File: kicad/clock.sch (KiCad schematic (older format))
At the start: 42 parts, among them Q1 PN2222A, Q2 PN2222A, Q3 PN2222A, Q4 PN2222A, Q5 PN2222A, Q6 PN2222A, U1 74HC04, U10 7SEGMENT_CC, U11 4543, U12 7SEGMENT_CC, U13 4543, U14 7SEGMENT_CC, U2 74LS390, U3 CD4060, U4 4543, U5 7SEGMENT_CC, U6 4027, U7 74LS390, U8 74LS390, U9 4543, Y1 32768

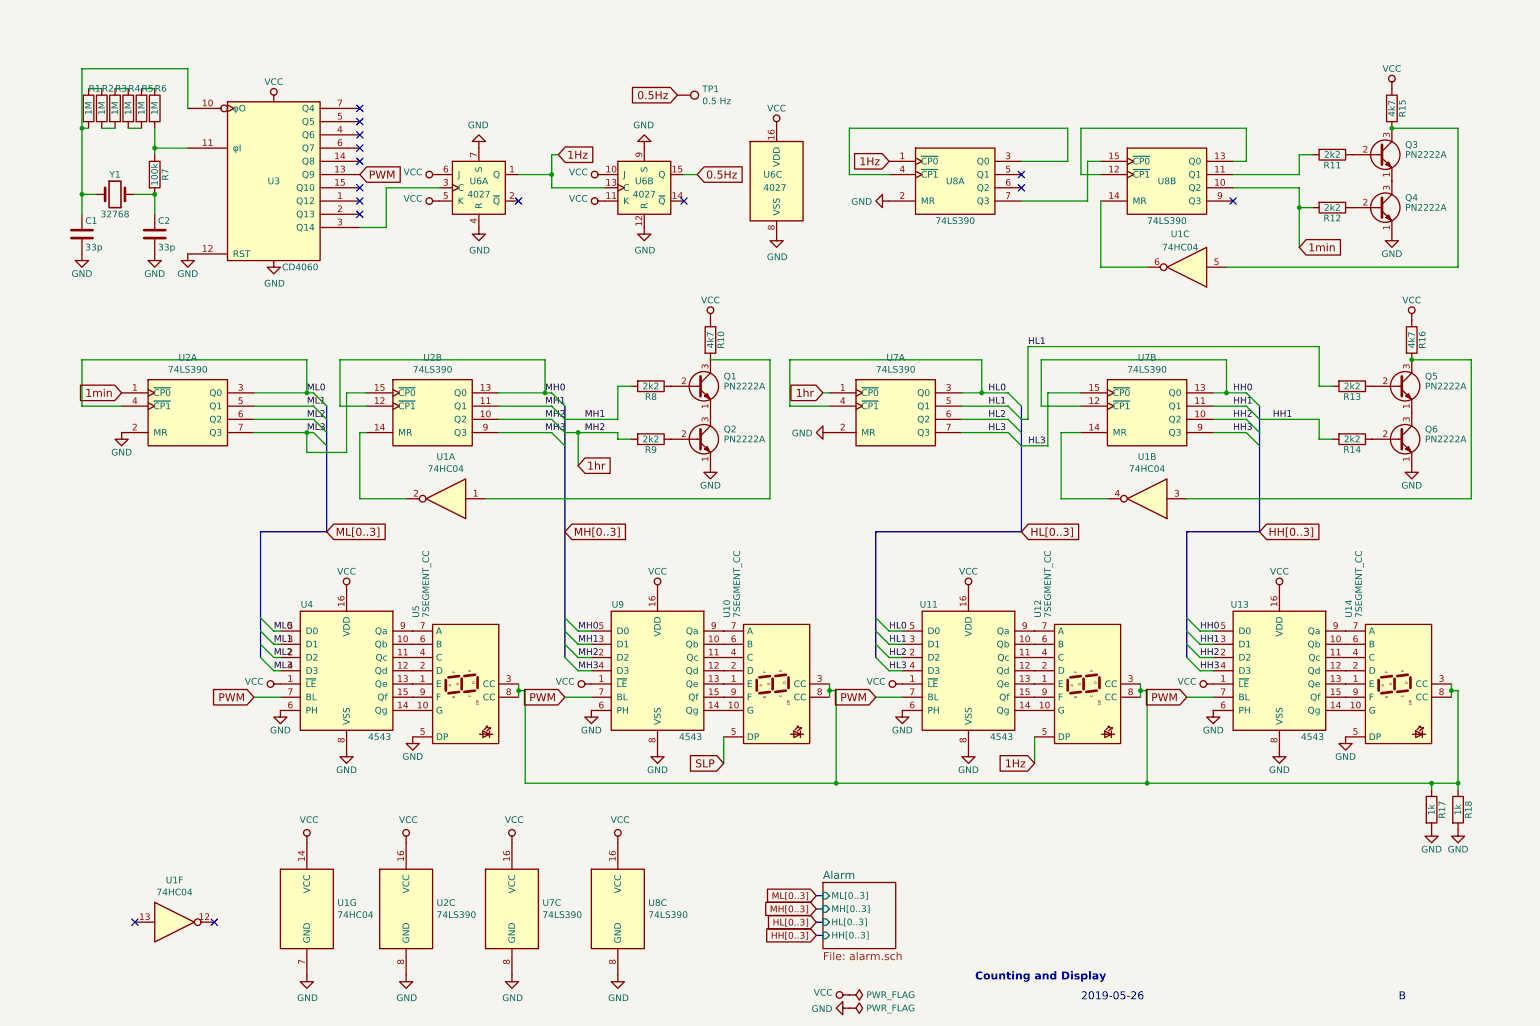
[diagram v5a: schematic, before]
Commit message: Routed switches
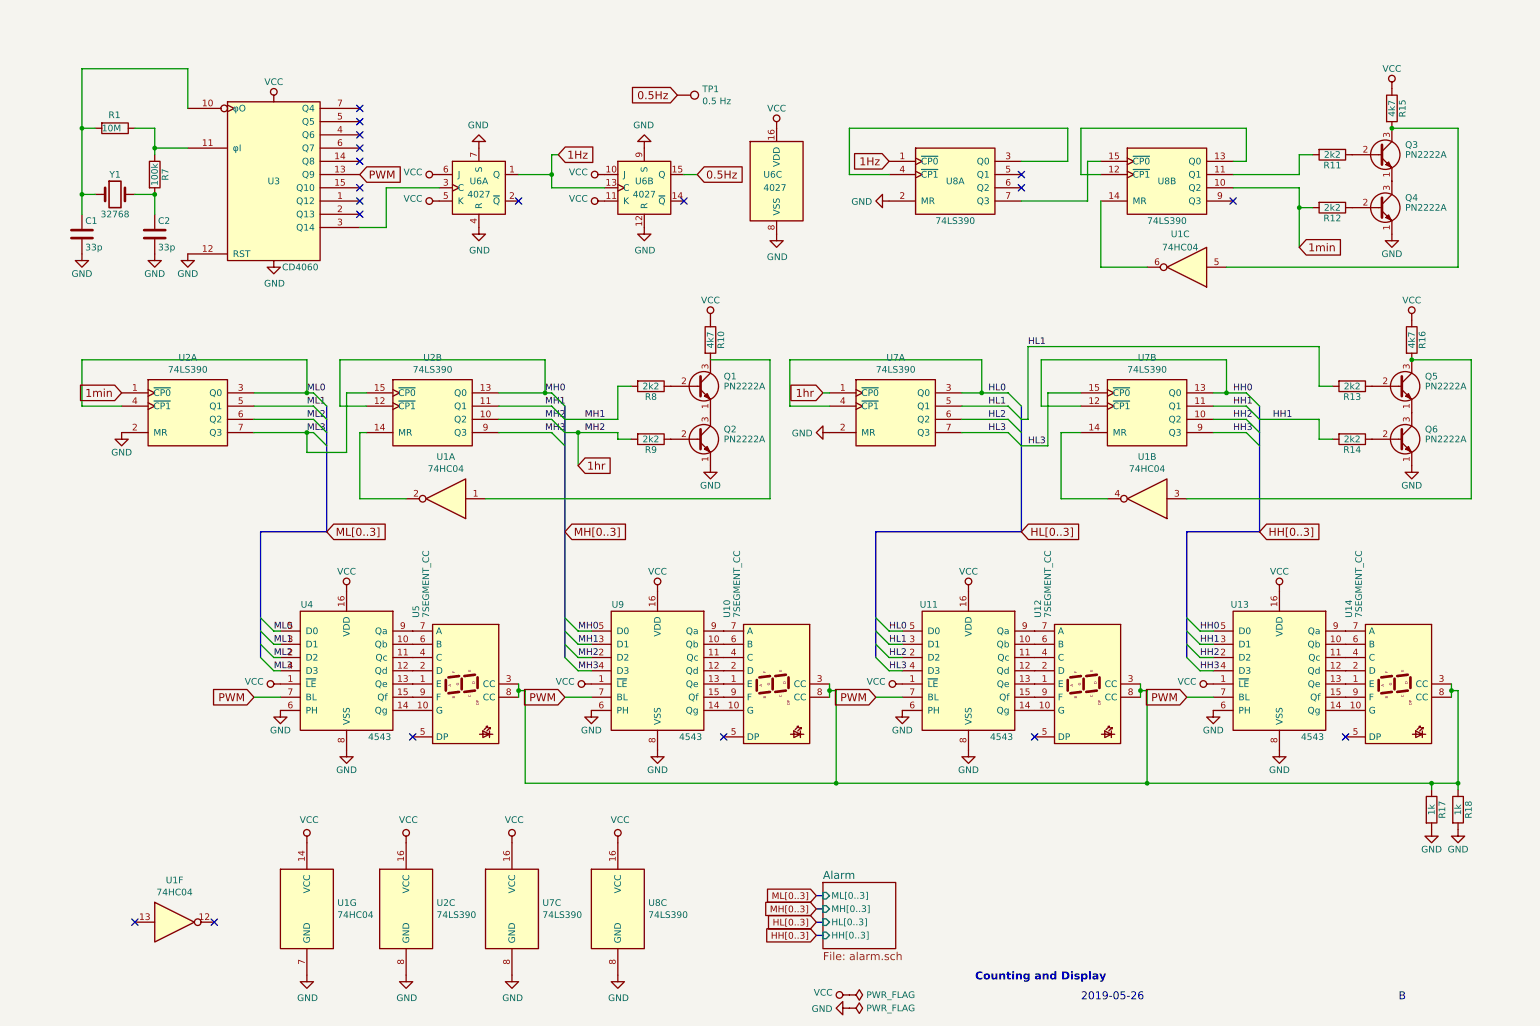
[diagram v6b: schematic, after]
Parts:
- removed R2, R3, R4, R5, R6: 1M, Resistors_THT:R_Axial_DIN0207_L6.3mm_D2.5mm_P10.16mm_Horizontal, symbol Device:R
- R1: value 1M -> 10M
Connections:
- net 1Hz: no longer U12.5 (DP)
- net GND: no longer U14.5 (DP), U5.5 (DP)
- net at R7.1, U3.11 (φI): now also R1.1
- net SLP: no longer names the net of U10.5 (DP)
- no-connect marks 15 -> 19
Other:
- moved on the sheet: R1
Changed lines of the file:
@@
 F5 "HL[0..3]" I L 6200 7050 50
 $EndSheet
-$Comp
-L power:GND #PWR048
-U 1 1 5CED9368
-P 10150 5650
-F 0 "#PWR048" H 10150 5400 50  0001 C CNN
-F 1 "GND" H 10150 5500 50  0000 C CNN
-F 2 "" H 10150 5650 50  0001 C CNN
-F 3 "" H 10150 5650 50  0001 C CNN
-	1    10150 5650
-	1    0    0    -1
-$EndComp
-$Comp
-L power:GND #PWR015
-U 1 1 5CED9423
-P 3100 5650
-F 0 "#PWR015" H 3100 5400 50  0001 C CNN
-F 1 "GND" H 3100 5500 50  0000 C CNN
-F 2 "" H 3100 5650 50  0001 C CNN
-F 3 "" H 3100 5650 50  0001 C CNN
-	1    3100 5650
-	1    0    0    -1
-$EndComp
-Text GLabel 7800 5850 0    60   Input ~ 0
-1Hz
-Wire Wire Line
-	7800 5850 7800 5650
-Wire Wire Line
-	5450 5650 5450 5850
-Text GLabel 5450 5850 0    60   Input ~ 0
-SLP
 Wire Wire Line
 	600  1550 600  1700
@@
 $EndComp
 $Comp
-L Device:R R6
-U 1 1 5D5D3111
-P 1150 900
-F 0 "R6" H 1150 1050 50  0000 L CNN
-F 1 "1M" V 1150 850 50  0000 L CNN
-F 2 "Resistors_THT:R_Axial_DIN0207_L6.3mm_D2.5mm_P10.16mm_Horizontal" V 1080 900 50  0001 C CNN
-F 3 "~" H 1150 900 50  0001 C CNN
-	1    1150 900
-	1    0    0    -1
-$EndComp
-$Comp
-L Device:R R5
-U 1 1 5D5D36CF
-P 1050 900
-F 0 "R5" H 1050 1050 50  0000 L CNN
-F 1 "1M" V 1050 850 50  0000 L CNN
-F 2 "Resistors_THT:R_Axial_DIN0207_L6.3mm_D2.5mm_P10.16mm_Horizontal" V 980 900 50  0001 C CNN
-F 3 "~" H 1050 900 50  0001 C CNN
-	1    1050 900
-	1    0    0    -1
-$EndComp
-$Comp
-L Device:R R4
-U 1 1 5D5D5655
-P 950 900
-F 0 "R4" H 950 1050 50  0000 L CNN
-F 1 "1M" V 950 850 50  0000 L CNN
-F 2 "Resistors_THT:R_Axial_DIN0207_L6.3mm_D2.5mm_P10.16mm_Horizontal" V 880 900 50  0001 C CNN
-F 3 "~" H 950 900 50  0001 C CNN
-	1    950  900
-	1    0    0    -1
-$EndComp
-$Comp
-L Device:R R3
-U 1 1 5D5D565B
-P 850 900
-F 0 "R3" H 850 1050 50  0000 L CNN
-F 1 "1M" V 850 850 50  0000 L CNN
-F 2 "Resistors_THT:R_Axial_DIN0207_L6.3mm_D2.5mm_P10.16mm_Horizontal" V 780 900 50  0001 C CNN
-F 3 "~" H 850 900 50  0001 C CNN
-	1    850  900
-	1    0    0    -1
-$EndComp
-$Comp
-L Device:R R2
-U 1 1 5D5DC362
-P 750 900
-F 0 "R2" H 750 1050 50  0000 L CNN
-F 1 "1M" V 750 850 50  0000 L CNN
-F 2 "Resistors_THT:R_Axial_DIN0207_L6.3mm_D2.5mm_P10.16mm_Horizontal" V 680 900 50  0001 C CNN
-F 3 "~" H 750 900 50  0001 C CNN
-	1    750  900
-	1    0    0    -1
-$EndComp
-$Comp
 L Device:R R1
 U 1 1 5D5DC368
-P 650 900
-F 0 "R1" H 650 1050 50  0000 L CNN
-F 1 "1M" V 650 850 50  0000 L CNN
-F 2 "Resistors_THT:R_Axial_DIN0207_L6.3mm_D2.5mm_P10.16mm_Horizontal" V 580 900 50  0001 C CNN
-F 3 "~" H 650 900 50  0001 C CNN
-	1    650  900
-	1    0    0    -1
+P 850 1050
+F 0 "R1" V 750 1000 50  0000 L CNN
+F 1 "10M" V 850 950 50  0000 L CNN
+F 2 "Resistors_THT:R_Axial_DIN0207_L6.3mm_D2.5mm_P10.16mm_Horizontal" V 780 1050 50  0001 C CNN
+F 3 "~" H 850 1050 50  0001 C CNN
+	1    850  1050
+	0    1    1    0
 $EndComp
 Connection ~ 1150 1550
@@
 Wire Wire Line
 	600  600  600  1050
-Wire Wire Line
-	1150 750  1050 750
-Wire Wire Line
-	1050 1050 950  1050
-Wire Wire Line
-	950  750  850  750
-Wire Wire Line
-	850  1050 750  1050
-Wire Wire Line
-	750  750  650  750
-Wire Wire Line
-	650  1050 600  1050
 Connection ~ 600  1050
 Wire Wire Line
@@
 	1    0    0    -1
 $EndComp
-Wire Bus Line
-	8950 4100 8950 5050
-Wire Bus Line
-	6600 4100 6600 5050
-Wire Bus Line
-	1950 4100 1950 5050
-Wire Bus Line
-	7700 3150 7700 4100
-Wire Bus Line
-	9500 3150 9500 4100
-Wire Bus Line
-	2450 3150 2450 4100
-Wire Bus Line
-	4250 3150 4250 5050
 Wire Wire Line
 	5150 1400 5250 1400
@@
 	0    1    1    0
 $EndComp
+Wire Wire Line
+	600  1050 700  1050
+Wire Wire Line
+	1000 1050 1150 1050
+NoConn ~ 3100 5650
+NoConn ~ 10150 5650
+NoConn ~ 7800 5650
+NoConn ~ 5450 5650
+Wire Bus Line
+	8950 4100 8950 5050
+Wire Bus Line
+	6600 4100 6600 5050
+Wire Bus Line
+	1950 4100 1950 5050
+Wire Bus Line
+	7700 3150 7700 4100
+Wire Bus Line
+	9500 3150 9500 4100
+Wire Bus Line
+	2450 3150 2450 4100
+Wire Bus Line
+	4250 3150 4250 5050
 $EndSCHEMATC

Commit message: Corrected schematic: SET button and discrete NAND blob
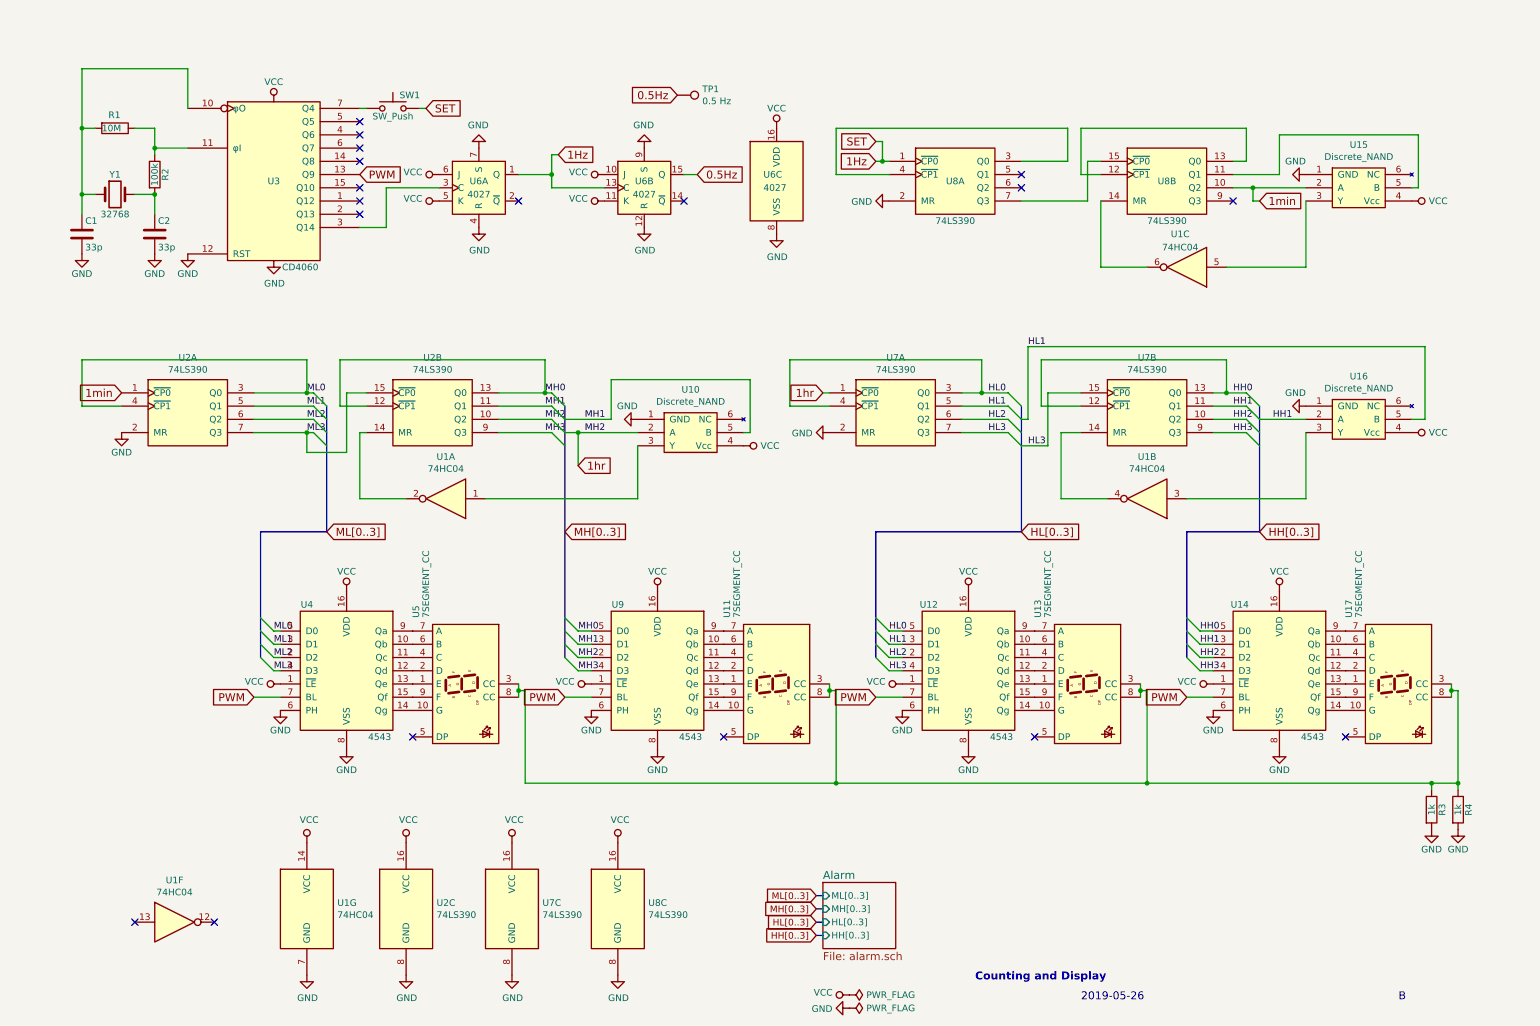
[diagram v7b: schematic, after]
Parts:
- removed Q1, Q2, Q3, Q4, Q5, Q6: PN2222A, TO_SOT_Packages_THT:TO-92_Molded_Narrow, symbol clock-rescue:PN2222A
- removed R10, R15, R16: 4k7, Resistors_THT:R_Axial_DIN0207_L6.3mm_D2.5mm_P10.16mm_Horizontal, symbol Device:R
- removed R11, R12, R13, R14, R8, R9: 2k2, Resistors_THT:R_Axial_DIN0207_L6.3mm_D2.5mm_P10.16mm_Horizontal, symbol Device:R
- added SW1: SW_Push, Buttons_Switches_THT:SW_TH_Tactile_Omron_B3F-10xx, symbol clock-rescue:SW_Push
- added U10, U15, U16: Discrete_NAND, Housings_DIP:DIP-6_W7.62mm, symbol clock:Discrete_NAND
- renumbered R7 to R2, R17 to R3, R18 to R4, U10 to U11, U11 to U12, U12 to U13, U13 to U14, U14 to U17
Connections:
- net 1Hz: now also SW1.2
- net 1hr: now also U10.2 (A)
- net 1min: now also U15.2 (A)
- net GND: now also U10.1 (GND), U15.1 (GND), U16.1 (GND)
- net HH1: now also U16.2 (A)
- net HL1: now also U16.5 (B)
- net MH1: now also U10.5 (B)
- net VCC: now also U10.4 (Vcc), U15.4 (Vcc), U16.4 (Vcc)
- net at U1.5: now also U15.3 (Y)
- net at U8.11 (Q1): now also U15.5 (B)
- net at U1.1: now also U10.3 (Y)
- net at U1.3: now also U16.3 (Y)
- net at U3.7 (Q4): now also SW1.1
- no-connect marks 19 -> 18

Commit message: Routing done: need board edges
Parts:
- added J1: Conn_01x02_Female, Wire_Pads:SolderWirePad_2x_1mmDrill, symbol Connector:Conn_01x02_Female
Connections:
- net GND: now also J1.2 (Pin_2)
- net VCC: now also J1.1 (Pin_1)
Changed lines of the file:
@@
 Wire Wire Line
 	3150 900  3200 900
+$Comp
+L power:VCC #PWR088
+U 1 1 5D784885
+P 850 5550
+F 0 "#PWR088" H 850 5400 50  0001 C CNN
+F 1 "VCC" H 867 5723 50  0000 C CNN
+F 2 "" H 850 5550 50  0001 C CNN
+F 3 "" H 850 5550 50  0001 C CNN
+	1    850  5550
+	1    0    0    -1
+$EndComp
+$Comp
+L power:GND #PWR089
+U 1 1 5D7851FE
+P 850 5950
+F 0 "#PWR089" H 850 5700 50  0001 C CNN
+F 1 "GND" H 855 5777 50  0000 C CNN
+F 2 "" H 850 5950 50  0001 C CNN
+F 3 "" H 850 5950 50  0001 C CNN
+	1    850  5950
+	1    0    0    -1
+$EndComp
+$Comp
+L Connector:Conn_01x02_Female J1
+U 1 1 5D777D7F
+P 1050 5700
+F 0 "J1" H 1078 5676 50  0000 L CNN
+F 1 "Conn_01x02_Female" H 1078 5585 50  0000 L CNN
+F 2 "Wire_Pads:SolderWirePad_2x_1mmDrill" H 1050 5700 50  0001 C CNN
+F 3 "~" H 1050 5700 50  0001 C CNN
+	1    1050 5700
+	1    0    0    -1
+$EndComp
+Wire Wire Line
+	850  5950 850  5800
+Wire Wire Line
+	850  5700 850  5550
 Wire Bus Line
 	8950 4100 8950 5050
